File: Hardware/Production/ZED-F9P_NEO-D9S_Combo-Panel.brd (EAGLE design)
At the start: 122.2 x 148.1 mm, 694 parts, among them J1 ANTENNA-SMA-GROUNDEDEDGE_SMA, J11 Qwiic Right Angle, J12 Qwiic Right Angle, J13 USB Female Type C Connector, J14 ANTENNA-SMA-GROUNDEDEDGE_SMA, J16 USB Female Type C Connector, J2 Qwiic Right Angle, J21 Qwiic Right Angle, J22 Qwiic Right Angle, J23 USB Female Type C Connector, J24 ANTENNA-SMA-GROUNDEDEDGE_SMA, J26 USB Female Type C Connector, J3 USB Female Type C Connector, J31 Qwiic Right Angle, J32 Qwiic Right Angle, J33 USB Female Type C Connector, J34 ANTENNA-SMA-GROUNDEDEDGE_SMA, J36 USB Female Type C Connector, J4 Qwiic Right Angle, J6 USB Female Type C Connector, U1 U-BLOX_NEO-D9S-00B, U10 U-BLOX_NEO-D9S-00B, U11 POWER-DIVIDER, U12 U-BLOX_ZED-F9P, U13 3.3V, U14 U-BLOX_NEO-D9S-00B, U15 POWER-DIVIDER, U16 U-BLOX_ZED-F9P, U2 3.3V, U3 POWER-DIVIDER, U4 U-BLOX_ZED-F9P, U5 3.3V, U6 U-BLOX_NEO-D9S-00B, U7 POWER-DIVIDER, U8 U-BLOX_ZED-F9P, U9 3.3V

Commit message: Add IC-16658 GNSS Power Divider. Delete New_parts.lbr
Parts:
- U11, U15, U3, U7: device New_Parts:PD0922J5050S2HF_ANA -> SparkFun-GPS:PD0922J5050S2HF_ANA
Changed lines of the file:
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@@
 <element name="U$58" library="output" package="#ANT_PWR#0" value="" x="36.83" y="61.468" smashed="yes" rot="MR90"/>
 <element name="U$59" library="output" package="#ANT_PWR#1" value="" x="36.83" y="61.468" smashed="yes" rot="R270"/>
-<element name="U3" library="New_Parts" package="PD0922J5050S2HF_ANA" value="POWER-DIVIDER" x="26.67" y="31.75" smashed="yes" rot="R270">
-<attribute name="DIGI-KEY_PART_NUMBER_1" value="1173-1094-2-ND" x="26.67" y="31.75" size="1.778" layer="27" ratio="15" rot="R270" display="off"/>
+<element name="U3" library="SparkFun-GPS" package="PD0922J5050S2HF_ANA" value="POWER-DIVIDER" x="26.67" y="31.75" smashed="yes" rot="R270">
 <attribute name="MANUFACTURER_PART_NUMBER" value="PD0922J5050S2HF" x="26.67" y="31.75" size="1.778" layer="27" ratio="15" rot="R270" display="off"/>
 <attribute name="NAME" x="27.686" y="32.893" size="0.508" layer="25" ratio="6" rot="SR270"/>
-<attribute name="PROD_ID" value="IC-16689" x="26.67" y="31.75" size="1.778" layer="27" ratio="15" rot="R270" display="off"/>
+<attribute name="PROD_ID" value="IC-16658" x="26.67" y="31.75" size="1.778" layer="27" ratio="15" rot="R270" display="off"/>
 <attribute name="VALUE" x="25.019" y="33.02" size="0.508" layer="27" ratio="6" rot="SR270"/>
 </element>
@@
 <element name="U$99" library="output" package="#ANT_PWR#0" value="" x="85.598" y="61.468" smashed="yes" rot="MR90"/>
 <element name="U$100" library="output" package="#ANT_PWR#1" value="" x="85.598" y="61.468" smashed="yes" rot="R270"/>
-<element name="U7" library="New_Parts" package="PD0922J5050S2HF_ANA" value="POWER-DIVIDER" x="75.438" y="31.75" smashed="yes" rot="R270">
-<attribute name="DIGI-KEY_PART_NUMBER_1" value="1173-1094-2-ND" x="75.438" y="31.75" size="1.778" layer="27" ratio="15" rot="R270" display="off"/>
+<element name="U7" library="SparkFun-GPS" package="PD0922J5050S2HF_ANA" value="POWER-DIVIDER" x="75.438" y="31.75" smashed="yes" rot="R270">
 <attribute name="MANUFACTURER_PART_NUMBER" value="PD0922J5050S2HF" x="75.438" y="31.75" size="1.778" layer="27" ratio="15" rot="R270" display="off"/>
 <attribute name="NAME" x="76.454" y="32.893" size="0.508" layer="25" ratio="6" rot="SR270"/>
-<attribute name="PROD_ID" value="IC-16689" x="75.438" y="31.75" size="1.778" layer="27" ratio="15" rot="R270" display="off"/>
+<attribute name="PROD_ID" value="IC-16658" x="75.438" y="31.75" size="1.778" layer="27" ratio="15" rot="R270" display="off"/>
 <attribute name="VALUE" x="73.787" y="33.02" size="0.508" layer="27" ratio="6" rot="SR270"/>
 </element>
@@
 <element name="U$177" library="output" package="#ANT_PWR#0" value="" x="36.83" y="125.476" smashed="yes" rot="MR90"/>
 <element name="U$178" library="output" package="#ANT_PWR#1" value="" x="36.83" y="125.476" smashed="yes" rot="R270"/>
-<element name="U11" library="New_Parts" package="PD0922J5050S2HF_ANA" value="POWER-DIVIDER" x="26.67" y="95.758" smashed="yes" rot="R270">
-<attribute name="DIGI-KEY_PART_NUMBER_1" value="1173-1094-2-ND" x="26.67" y="95.758" size="1.778" layer="27" ratio="15" rot="R270" display="off"/>
+<element name="U11" library="SparkFun-GPS" package="PD0922J5050S2HF_ANA" value="POWER-DIVIDER" x="26.67" y="95.758" smashed="yes" rot="R270">
 <attribute name="MANUFACTURER_PART_NUMBER" value="PD0922J5050S2HF" x="26.67" y="95.758" size="1.778" layer="27" ratio="15" rot="R270" display="off"/>
 <attribute name="NAME" x="27.686" y="96.901" size="0.508" layer="25" ratio="6" rot="SR270"/>
-<attribute name="PROD_ID" value="IC-16689" x="26.67" y="95.758" size="1.778" layer="27" ratio="15" rot="R270" display="off"/>
+<attribute name="PROD_ID" value="IC-16658" x="26.67" y="95.758" size="1.778" layer="27" ratio="15" rot="R270" display="off"/>
 <attribute name="VALUE" x="25.019" y="97.028" size="0.508" layer="27" ratio="6" rot="SR270"/>
 </element>
@@
 <element name="U$255" library="output" package="#ANT_PWR#0" value="" x="85.598" y="125.476" smashed="yes" rot="MR90"/>
 <element name="U$256" library="output" package="#ANT_PWR#1" value="" x="85.598" y="125.476" smashed="yes" rot="R270"/>
-<element name="U15" library="New_Parts" package="PD0922J5050S2HF_ANA" value="POWER-DIVIDER" x="75.438" y="95.758" smashed="yes" rot="R270">
-<attribute name="DIGI-KEY_PART_NUMBER_1" value="1173-1094-2-ND" x="75.438" y="95.758" size="1.778" layer="27" ratio="15" rot="R270" display="off"/>
+<element name="U15" library="SparkFun-GPS" package="PD0922J5050S2HF_ANA" value="POWER-DIVIDER" x="75.438" y="95.758" smashed="yes" rot="R270">
 <attribute name="MANUFACTURER_PART_NUMBER" value="PD0922J5050S2HF" x="75.438" y="95.758" size="1.778" layer="27" ratio="15" rot="R270" display="off"/>
 <attribute name="NAME" x="76.454" y="96.901" size="0.508" layer="25" ratio="6" rot="SR270"/>
-<attribute name="PROD_ID" value="IC-16689" x="75.438" y="95.758" size="1.778" layer="27" ratio="15" rot="R270" display="off"/>
+<attribute name="PROD_ID" value="IC-16658" x="75.438" y="95.758" size="1.778" layer="27" ratio="15" rot="R270" display="off"/>
 <attribute name="VALUE" x="73.787" y="97.028" size="0.508" layer="27" ratio="6" rot="SR270"/>
 </element>

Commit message: Use RF Library copy of IC-16658
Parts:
- U11, U15, U3, U7: device SparkFun-GPS:PD0922J5050S2HF_ANA -> SparkFun-RF:PD0922J5050S2HF_ANA
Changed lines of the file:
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@@
 <element name="U$58" library="output" package="#ANT_PWR#0" value="" x="36.83" y="61.468" smashed="yes" rot="MR90"/>
 <element name="U$59" library="output" package="#ANT_PWR#1" value="" x="36.83" y="61.468" smashed="yes" rot="R270"/>
-<element name="U3" library="SparkFun-GPS" package="PD0922J5050S2HF_ANA" value="POWER-DIVIDER" x="26.67" y="31.75" smashed="yes" rot="R270">
+<element name="U3" library="SparkFun-RF" package="PD0922J5050S2HF_ANA" value="POWER-DIVIDER" x="26.67" y="31.75" smashed="yes" rot="R270">
+<attribute name="DIGI-KEY_PART_NUMBER_1" value="1173-1094-2-ND" x="26.67" y="31.75" size="1.778" layer="27" rot="R270" display="off"/>
 <attribute name="MANUFACTURER_PART_NUMBER" value="PD0922J5050S2HF" x="26.67" y="31.75" size="1.778" layer="27" ratio="15" rot="R270" display="off"/>
 <attribute name="NAME" x="27.686" y="32.893" size="0.508" layer="25" ratio="6" rot="SR270"/>
@@
 <element name="U$99" library="output" package="#ANT_PWR#0" value="" x="85.598" y="61.468" smashed="yes" rot="MR90"/>
 <element name="U$100" library="output" package="#ANT_PWR#1" value="" x="85.598" y="61.468" smashed="yes" rot="R270"/>
-<element name="U7" library="SparkFun-GPS" package="PD0922J5050S2HF_ANA" value="POWER-DIVIDER" x="75.438" y="31.75" smashed="yes" rot="R270">
+<element name="U7" library="SparkFun-RF" package="PD0922J5050S2HF_ANA" value="POWER-DIVIDER" x="75.438" y="31.75" smashed="yes" rot="R270">
+<attribute name="DIGI-KEY_PART_NUMBER_1" value="1173-1094-2-ND" x="75.438" y="31.75" size="1.778" layer="27" rot="R270" display="off"/>
 <attribute name="MANUFACTURER_PART_NUMBER" value="PD0922J5050S2HF" x="75.438" y="31.75" size="1.778" layer="27" ratio="15" rot="R270" display="off"/>
 <attribute name="NAME" x="76.454" y="32.893" size="0.508" layer="25" ratio="6" rot="SR270"/>
@@
 <element name="U$177" library="output" package="#ANT_PWR#0" value="" x="36.83" y="125.476" smashed="yes" rot="MR90"/>
 <element name="U$178" library="output" package="#ANT_PWR#1" value="" x="36.83" y="125.476" smashed="yes" rot="R270"/>
-<element name="U11" library="SparkFun-GPS" package="PD0922J5050S2HF_ANA" value="POWER-DIVIDER" x="26.67" y="95.758" smashed="yes" rot="R270">
+<element name="U11" library="SparkFun-RF" package="PD0922J5050S2HF_ANA" value="POWER-DIVIDER" x="26.67" y="95.758" smashed="yes" rot="R270">
+<attribute name="DIGI-KEY_PART_NUMBER_1" value="1173-1094-2-ND" x="26.67" y="95.758" size="1.778" layer="27" rot="R270" display="off"/>
 <attribute name="MANUFACTURER_PART_NUMBER" value="PD0922J5050S2HF" x="26.67" y="95.758" size="1.778" layer="27" ratio="15" rot="R270" display="off"/>
 <attribute name="NAME" x="27.686" y="96.901" size="0.508" layer="25" ratio="6" rot="SR270"/>
@@
 <element name="U$255" library="output" package="#ANT_PWR#0" value="" x="85.598" y="125.476" smashed="yes" rot="MR90"/>
 <element name="U$256" library="output" package="#ANT_PWR#1" value="" x="85.598" y="125.476" smashed="yes" rot="R270"/>
-<element name="U15" library="SparkFun-GPS" package="PD0922J5050S2HF_ANA" value="POWER-DIVIDER" x="75.438" y="95.758" smashed="yes" rot="R270">
+<element name="U15" library="SparkFun-RF" package="PD0922J5050S2HF_ANA" value="POWER-DIVIDER" x="75.438" y="95.758" smashed="yes" rot="R270">
+<attribute name="DIGI-KEY_PART_NUMBER_1" value="1173-1094-2-ND" x="75.438" y="95.758" size="1.778" layer="27" rot="R270" display="off"/>
 <attribute name="MANUFACTURER_PART_NUMBER" value="PD0922J5050S2HF" x="75.438" y="95.758" size="1.778" layer="27" ratio="15" rot="R270" display="off"/>
 <attribute name="NAME" x="76.454" y="96.901" size="0.508" layer="25" ratio="6" rot="SR270"/>

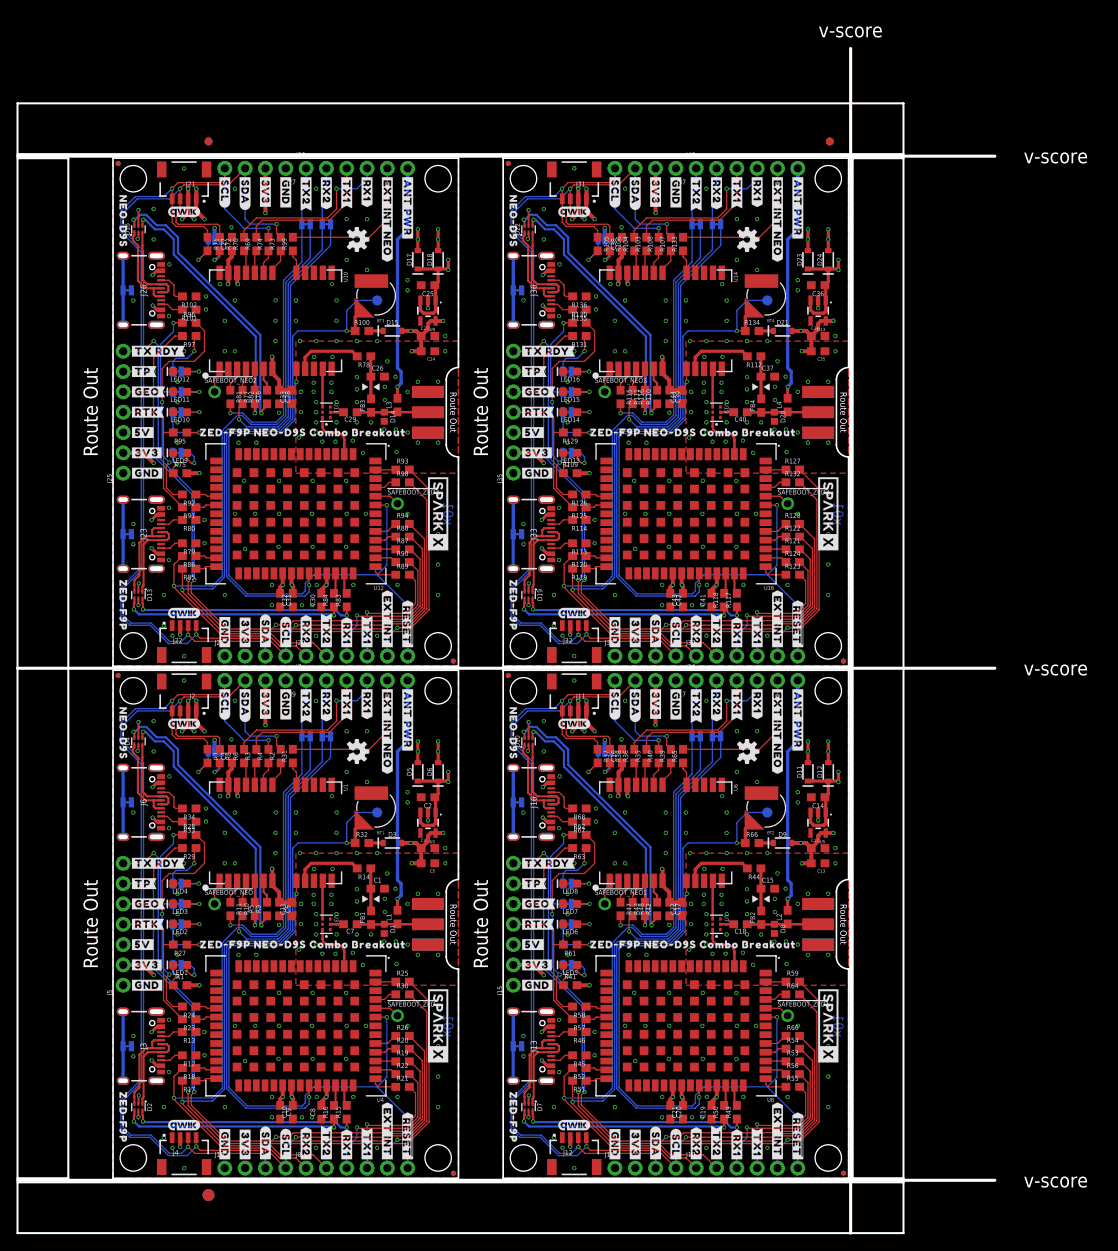
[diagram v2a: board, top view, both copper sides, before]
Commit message: x02 PCB - inverts RTK LED
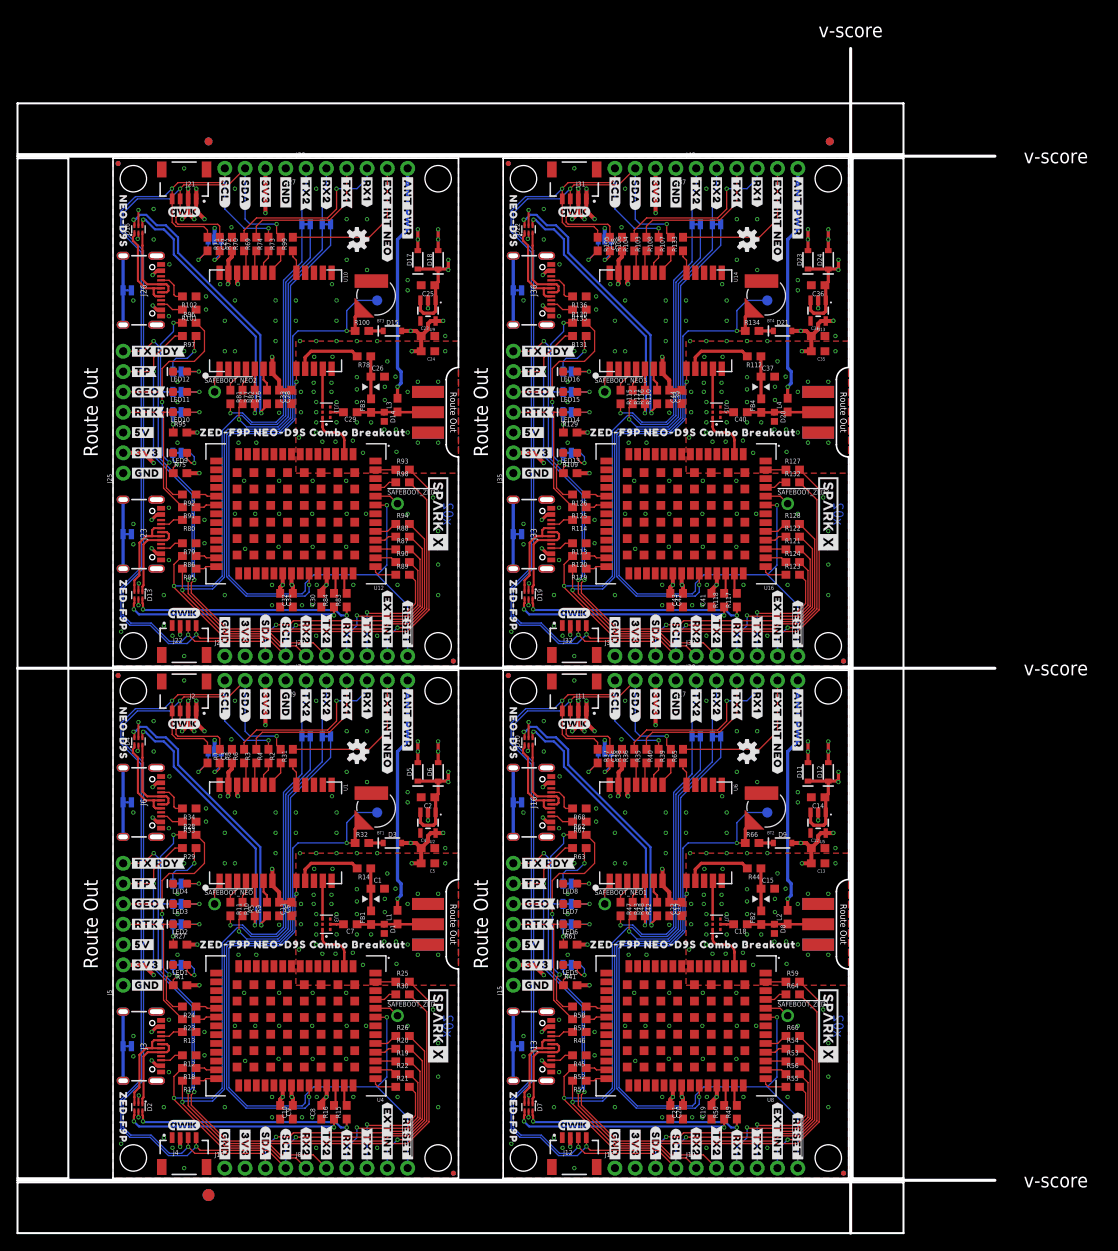
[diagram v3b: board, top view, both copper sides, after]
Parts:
- turned R129 to 0 degrees
- turned R27 to 0 degrees
- turned R61 to 0 degrees
- turned R95 to 0 degrees
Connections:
- net 3.3V: now also R27.2
- net 3.3V1: now also R61.2
- net 3.3V2: now also R95.2
- net 3.3V3: now also R129.2
- net GND: no longer LED2.C
- net GND1: no longer LED6.C
- net GND2: no longer LED10.C
- net GND3: no longer LED14.C
- net RTK: now also LED2.C; no longer R27.2
- net RTK1: now also LED6.C; no longer R61.2
- net RTK2: now also LED10.C; no longer R95.2
- net RTK3: now also LED14.C; no longer R129.2
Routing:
- net N$136: track 7.11 -> 2.56 mm
- net N$62: track 7.11 -> 2.56 mm
- net N$99: track 7.11 -> 2.56 mm
- net N$28: track 7.11 -> 2.56 mm
- net 3.3V3: track 49.0 -> 50.3 mm, vias 17 -> 18
- net 3.3V2: track 49.0 -> 50.3 mm, vias 17 -> 18
- net 3.3V1: track 49.0 -> 50.3 mm, vias 17 -> 18
- net 3.3V: track 49.0 -> 50.3 mm, vias 17 -> 18
- net GND3: vias 127 -> 126
- net GND2: vias 127 -> 126
- net GND1: vias 127 -> 126
- net GND: vias 127 -> 126
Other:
- board text added: "x02"
- board text removed: "x01"
